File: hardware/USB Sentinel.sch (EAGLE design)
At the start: 35 parts, among them J1 USB+SHIELD-MICROB, J2 USB+SHIELD-A-S, U1 ATMEGA32U2-QFN32, U3 MAX3421EETJ+, Y1 8MHz, Y2 12MHz

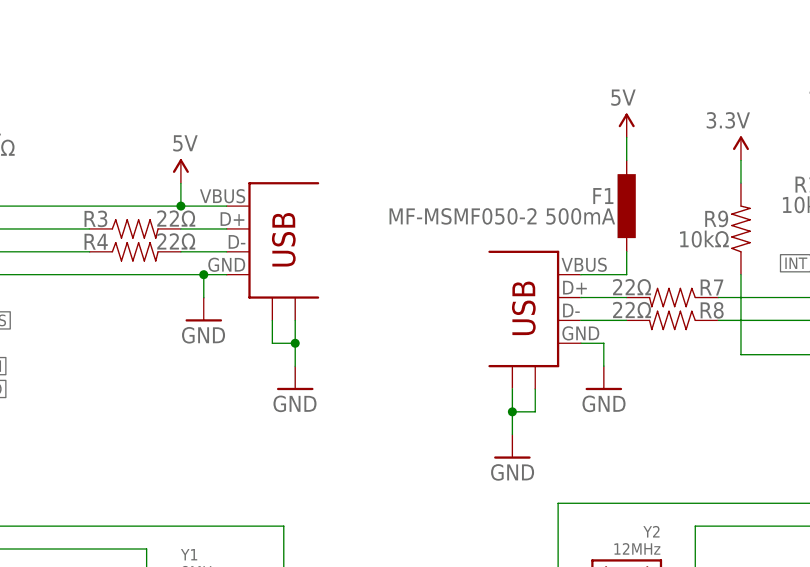
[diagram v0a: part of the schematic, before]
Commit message: Updated PCB
Changed a few things on the PCB to help with production.
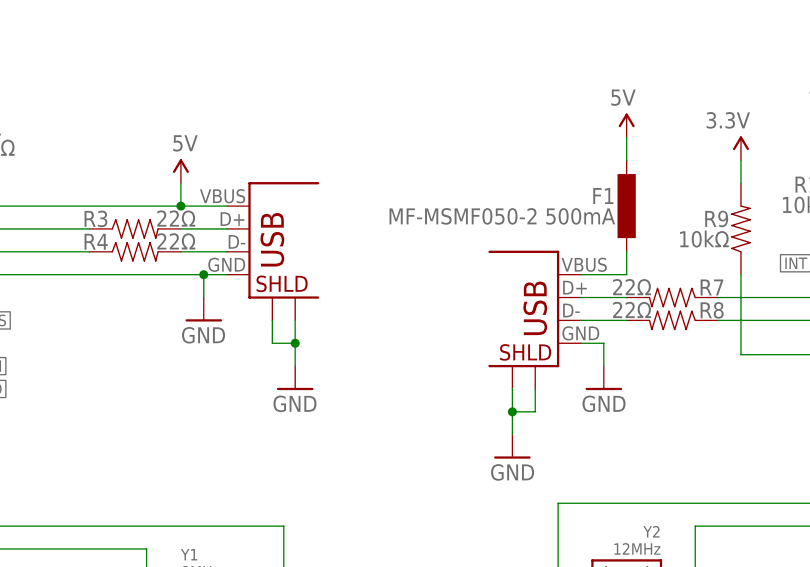
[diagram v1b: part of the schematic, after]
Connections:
- net GND: now also J1.P$1, J1.P$2, J2.P$1, J2.P$2; no longer J1.S1, J1.S2, J2.S1, J2.S2
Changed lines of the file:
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@@
 <setting verticaltext="up"/>
 </settings>
-<grid distance="0.05" unitdist="inch" unit="inch" style="lines" multiple="1" display="yes" altdistance="0.01" altunitdist="inch" altunit="inch"/>
+<grid distance="0.1" unitdist="inch" unit="inch" style="lines" multiple="1" display="no" altdistance="0.01" altunitdist="inch" altunit="inch"/>
 <layers>
 <layer number="1" name="Top" color="4" fill="1" visible="no" active="no"/>
@@
 </segment>
 <segment>
-<pinref part="J1" gate="G$1" pin="S2"/>
+<pinref part="J1" gate="G$1" pin="P$2"/>
 <pinref part="GND5" gate="G$1" pin="GND"/>
 <wire x1="45.72" y1="17.78" x2="45.72" y2="15.24" width="0.1524" layer="91"/>
-<pinref part="J1" gate="G$1" pin="S1"/>
+<pinref part="J1" gate="G$1" pin="P$1"/>
 <wire x1="45.72" y1="15.24" x2="45.72" y2="12.7" width="0.1524" layer="91"/>
 <wire x1="45.72" y1="15.24" x2="43.18" y2="15.24" width="0.1524" layer="91"/>
@@
 </segment>
 <segment>
-<pinref part="J2" gate="G$1" pin="S2"/>
+<pinref part="J2" gate="G$1" pin="P$2"/>
 <pinref part="GND11" gate="G$1" pin="GND"/>
 <wire x1="69.85" y1="10.16" x2="69.85" y2="7.62" width="0.1524" layer="91"/>
-<pinref part="J2" gate="G$1" pin="S1"/>
+<pinref part="J2" gate="G$1" pin="P$1"/>
 <wire x1="69.85" y1="7.62" x2="69.85" y2="5.08" width="0.1524" layer="91"/>
 <wire x1="69.85" y1="7.62" x2="72.39" y2="7.62" width="0.1524" layer="91"/>
